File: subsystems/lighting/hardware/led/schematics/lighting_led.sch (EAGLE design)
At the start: 17 parts, among them J1 MOLEX-MICROLOCK-6PIN, J2 MOLEX-MICROLOCK-6PIN

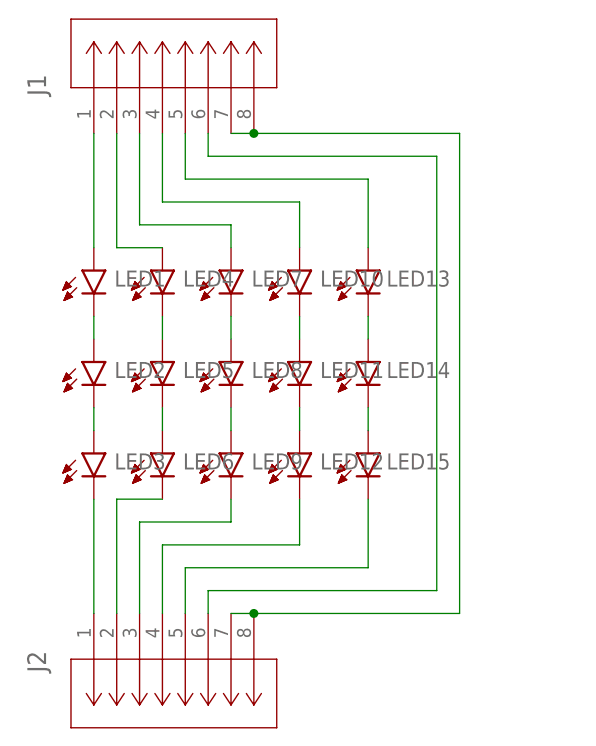
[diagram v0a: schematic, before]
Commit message: Lighting V0.3
Fixed daisy-chaining "mirroring" problem
Made DC jack footprint holes smaller (3.3mm->3.1mm dia.)
Made Molex support pads NC
Minor routing updates
Updated silkscreen text
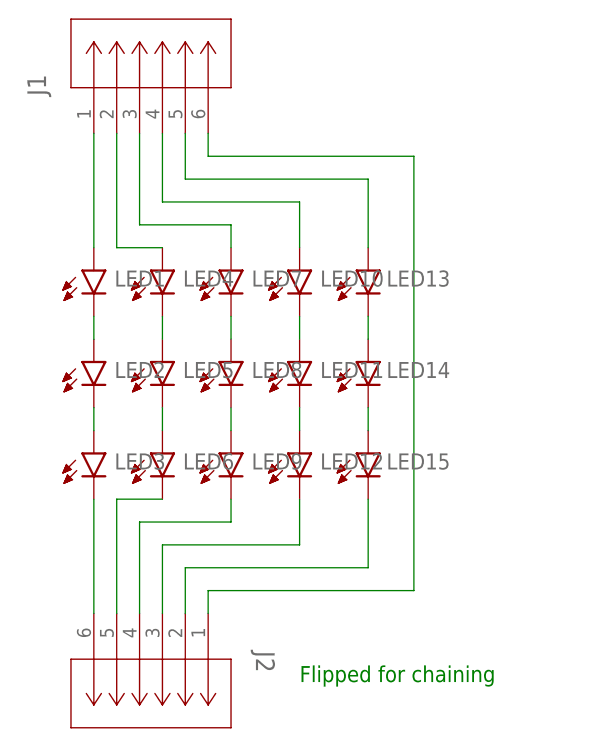
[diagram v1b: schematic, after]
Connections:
- removed net N$17: J1.7, J1.8, J2.7, J2.8
- net N$16: now also J2.1; no longer J2.6
- net N$18: now also J2.2; no longer J2.5
- net N$19: now also J2.3; no longer J2.4
- net N$20: now also J2.4; no longer J2.3
- net N$21: now also J2.5; no longer J2.2
- net N$22: now also J2.6; no longer J2.1
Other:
- note added: "Flipped for chaining"
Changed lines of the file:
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@@
 <sheet>
 <plain>
+<text x="71.12" y="20.32" size="1.778" layer="91">Flipped for chaining</text>
 </plain>
 <instances>
@@
 <attribute name="NAME" x="42.9514" y="85.4456" size="2.0828" layer="95" ratio="6" rot="SR90"/>
 </instance>
-<instance part="J2" gate="G$1" x="48.26" y="27.94" smashed="yes" rot="MR270">
-<attribute name="NAME" x="42.9514" y="23.7744" size="2.0828" layer="95" ratio="6" rot="SMR270"/>
+<instance part="J2" gate="G$1" x="60.96" y="27.94" smashed="yes" rot="R270">
+<attribute name="NAME" x="66.2686" y="23.7744" size="2.0828" layer="95" ratio="6" rot="SR270"/>
 </instance>
 </instances>
@@
 <segment>
 <wire x1="60.96" y1="81.28" x2="60.96" y2="78.74" width="0.1524" layer="91"/>
-<wire x1="60.96" y1="78.74" x2="86.36" y2="78.74" width="0.1524" layer="91"/>
-<wire x1="86.36" y1="78.74" x2="86.36" y2="30.48" width="0.1524" layer="91"/>
-<wire x1="86.36" y1="30.48" x2="60.96" y2="30.48" width="0.1524" layer="91"/>
+<pinref part="J1" gate="G$1" pin="6"/>
+<wire x1="60.96" y1="78.74" x2="83.82" y2="78.74" width="0.1524" layer="91"/>
+<wire x1="83.82" y1="78.74" x2="83.82" y2="30.48" width="0.1524" layer="91"/>
+<wire x1="83.82" y1="30.48" x2="60.96" y2="30.48" width="0.1524" layer="91"/>
 <wire x1="60.96" y1="30.48" x2="60.96" y2="27.94" width="0.1524" layer="91"/>
-<pinref part="J1" gate="G$1" pin="6"/>
-<pinref part="J2" gate="G$1" pin="6"/>
-</segment>
-</net>
-<net name="N$17" class="0">
-<segment>
-<wire x1="88.9" y1="81.28" x2="88.9" y2="27.94" width="0.1524" layer="91"/>
-<wire x1="66.04" y1="81.28" x2="88.9" y2="81.28" width="0.1524" layer="91"/>
-<pinref part="J1" gate="G$1" pin="8"/>
-<wire x1="88.9" y1="27.94" x2="66.04" y2="27.94" width="0.1524" layer="91"/>
-<pinref part="J2" gate="G$1" pin="8"/>
-<wire x1="66.04" y1="81.28" x2="63.5" y2="81.28" width="0.1524" layer="91"/>
-<junction x="66.04" y="81.28"/>
-<pinref part="J1" gate="G$1" pin="7"/>
-<wire x1="66.04" y1="27.94" x2="63.5" y2="27.94" width="0.1524" layer="91"/>
-<junction x="66.04" y="27.94"/>
-<pinref part="J2" gate="G$1" pin="7"/>
+<pinref part="J2" gate="G$1" pin="1"/>
 </segment>
 </net>
@@
 <wire x1="78.74" y1="33.02" x2="78.74" y2="40.64" width="0.1524" layer="91"/>
 <pinref part="LED15" gate="G$1" pin="C"/>
-<pinref part="J2" gate="G$1" pin="5"/>
+<pinref part="J2" gate="G$1" pin="2"/>
 </segment>
 </net>
@@
 <wire x1="55.88" y1="35.56" x2="55.88" y2="27.94" width="0.1524" layer="91"/>
 <pinref part="LED12" gate="G$1" pin="C"/>
-<pinref part="J2" gate="G$1" pin="4"/>
+<pinref part="J2" gate="G$1" pin="3"/>
 </segment>
 </net>
@@
 <wire x1="53.34" y1="38.1" x2="53.34" y2="27.94" width="0.1524" layer="91"/>
 <pinref part="LED9" gate="G$1" pin="C"/>
-<pinref part="J2" gate="G$1" pin="3"/>
+<pinref part="J2" gate="G$1" pin="4"/>
 </segment>
 </net>
@@
 <wire x1="50.8" y1="40.64" x2="50.8" y2="27.94" width="0.1524" layer="91"/>
 <pinref part="LED6" gate="G$1" pin="C"/>
-<pinref part="J2" gate="G$1" pin="2"/>
+<pinref part="J2" gate="G$1" pin="5"/>
 </segment>
 </net>
@@
 <wire x1="48.26" y1="40.64" x2="48.26" y2="27.94" width="0.1524" layer="91"/>
 <pinref part="LED3" gate="G$1" pin="C"/>
-<pinref part="J2" gate="G$1" pin="1"/>
-</segment>
-</net>
+<pinref part="J2" gate="G$1" pin="6"/>
+</segment>
+</net>

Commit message: Lighting V0.4
FINALLY fixed the connector flipping error (hint: pin 1 goes to pin 6 EVERY TIME)
Flipped LED series order (blue on bottom)
More "bus"-like routing on power PCB
Updated version number text on PCBs
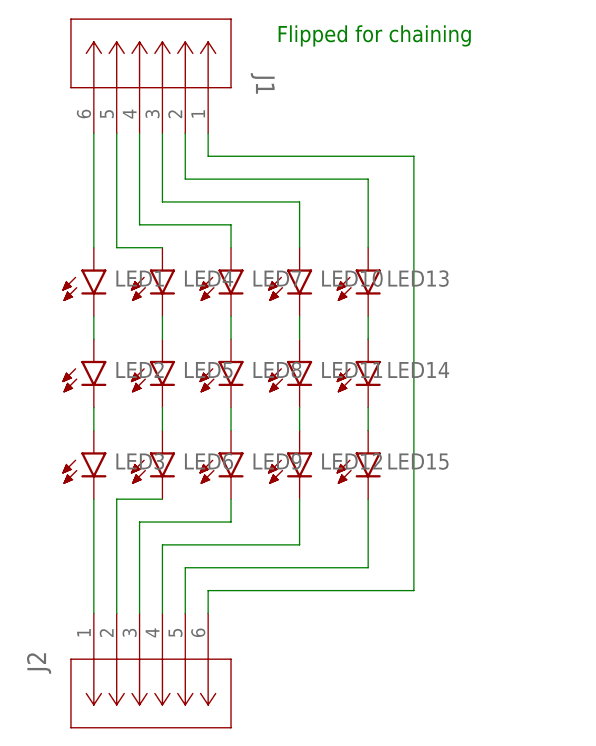
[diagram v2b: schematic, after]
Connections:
- net N$11: now also J1.6; no longer J1.1
- net N$12: now also J1.5; no longer J1.2
- net N$13: now also J1.4; no longer J1.3
- net N$14: now also J1.3; no longer J1.4
- net N$15: now also J1.2; no longer J1.5
- net N$16: now also J1.1, J2.6; no longer J1.6, J2.1
- net N$18: now also J2.5; no longer J2.2
- net N$19: now also J2.4; no longer J2.3
- net N$20: now also J2.3; no longer J2.4
- net N$21: now also J2.2; no longer J2.5
- net N$22: now also J2.1; no longer J2.6
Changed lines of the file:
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@@
 <sheet>
 <plain>
-<text x="71.12" y="20.32" size="1.778" layer="91">Flipped for chaining</text>
+<text x="68.58" y="91.44" size="1.778" layer="91">Flipped for chaining</text>
 </plain>
 <instances>
@@
 <attribute name="NAME" x="65.786" y="43.942" size="1.778" layer="95" rot="R180" align="top-right"/>
 </instance>
-<instance part="J1" gate="G$1" x="48.26" y="81.28" smashed="yes" rot="R90">
-<attribute name="NAME" x="42.9514" y="85.4456" size="2.0828" layer="95" ratio="6" rot="SR90"/>
-</instance>
-<instance part="J2" gate="G$1" x="60.96" y="27.94" smashed="yes" rot="R270">
-<attribute name="NAME" x="66.2686" y="23.7744" size="2.0828" layer="95" ratio="6" rot="SR270"/>
+<instance part="J1" gate="G$1" x="60.96" y="81.28" smashed="yes" rot="MR90">
+<attribute name="NAME" x="66.2686" y="85.4456" size="2.0828" layer="95" ratio="6" rot="SMR90"/>
+</instance>
+<instance part="J2" gate="G$1" x="48.26" y="27.94" smashed="yes" rot="MR270">
+<attribute name="NAME" x="42.9514" y="23.7744" size="2.0828" layer="95" ratio="6" rot="SMR270"/>
 </instance>
 </instances>
@@
 <wire x1="48.26" y1="81.28" x2="48.26" y2="68.58" width="0.1524" layer="91"/>
 <pinref part="LED1" gate="G$1" pin="A"/>
-<pinref part="J1" gate="G$1" pin="1"/>
+<pinref part="J1" gate="G$1" pin="6"/>
 </segment>
 </net>
@@
 <wire x1="50.8" y1="68.58" x2="55.88" y2="68.58" width="0.1524" layer="91"/>
 <pinref part="LED4" gate="G$1" pin="A"/>
-<pinref part="J1" gate="G$1" pin="2"/>
+<pinref part="J1" gate="G$1" pin="5"/>
 </segment>
 </net>
@@
 <wire x1="63.5" y1="71.12" x2="63.5" y2="68.58" width="0.1524" layer="91"/>
 <pinref part="LED7" gate="G$1" pin="A"/>
-<pinref part="J1" gate="G$1" pin="3"/>
+<pinref part="J1" gate="G$1" pin="4"/>
 </segment>
 </net>
@@
 <wire x1="71.12" y1="73.66" x2="71.12" y2="68.58" width="0.1524" layer="91"/>
 <pinref part="LED10" gate="G$1" pin="A"/>
-<pinref part="J1" gate="G$1" pin="4"/>
+<pinref part="J1" gate="G$1" pin="3"/>
 </segment>
 </net>
@@
 <wire x1="78.74" y1="76.2" x2="78.74" y2="68.58" width="0.1524" layer="91"/>
 <pinref part="LED13" gate="G$1" pin="A"/>
-<pinref part="J1" gate="G$1" pin="5"/>
+<pinref part="J1" gate="G$1" pin="2"/>
 </segment>
 </net>
@@
 <segment>
 <wire x1="60.96" y1="81.28" x2="60.96" y2="78.74" width="0.1524" layer="91"/>
-<pinref part="J1" gate="G$1" pin="6"/>
 <wire x1="60.96" y1="78.74" x2="83.82" y2="78.74" width="0.1524" layer="91"/>
 <wire x1="83.82" y1="78.74" x2="83.82" y2="30.48" width="0.1524" layer="91"/>
 <wire x1="83.82" y1="30.48" x2="60.96" y2="30.48" width="0.1524" layer="91"/>
 <wire x1="60.96" y1="30.48" x2="60.96" y2="27.94" width="0.1524" layer="91"/>
-<pinref part="J2" gate="G$1" pin="1"/>
+<pinref part="J1" gate="G$1" pin="1"/>
+<pinref part="J2" gate="G$1" pin="6"/>
 </segment>
 </net>
@@
 <wire x1="78.74" y1="33.02" x2="78.74" y2="40.64" width="0.1524" layer="91"/>
 <pinref part="LED15" gate="G$1" pin="C"/>
-<pinref part="J2" gate="G$1" pin="2"/>
+<pinref part="J2" gate="G$1" pin="5"/>
 </segment>
 </net>
@@
 <wire x1="55.88" y1="35.56" x2="55.88" y2="27.94" width="0.1524" layer="91"/>
 <pinref part="LED12" gate="G$1" pin="C"/>
-<pinref part="J2" gate="G$1" pin="3"/>
+<pinref part="J2" gate="G$1" pin="4"/>
 </segment>
 </net>
@@
 <wire x1="53.34" y1="38.1" x2="53.34" y2="27.94" width="0.1524" layer="91"/>
 <pinref part="LED9" gate="G$1" pin="C"/>
-<pinref part="J2" gate="G$1" pin="4"/>
+<pinref part="J2" gate="G$1" pin="3"/>
 </segment>
 </net>
@@
 <wire x1="50.8" y1="40.64" x2="50.8" y2="27.94" width="0.1524" layer="91"/>
 <pinref part="LED6" gate="G$1" pin="C"/>
-<pinref part="J2" gate="G$1" pin="5"/>
+<pinref part="J2" gate="G$1" pin="2"/>
 </segment>
 </net>
@@
 <wire x1="48.26" y1="40.64" x2="48.26" y2="27.94" width="0.1524" layer="91"/>
 <pinref part="LED3" gate="G$1" pin="C"/>
-<pinref part="J2" gate="G$1" pin="6"/>
-</segment>
-</net>
+<pinref part="J2" gate="G$1" pin="1"/>
+</segment>
+</net>
